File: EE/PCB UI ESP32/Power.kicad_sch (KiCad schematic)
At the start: 7 parts, among them J2 T1M-02-F-SV-L, U12 MCP1826ST-3302E_DB

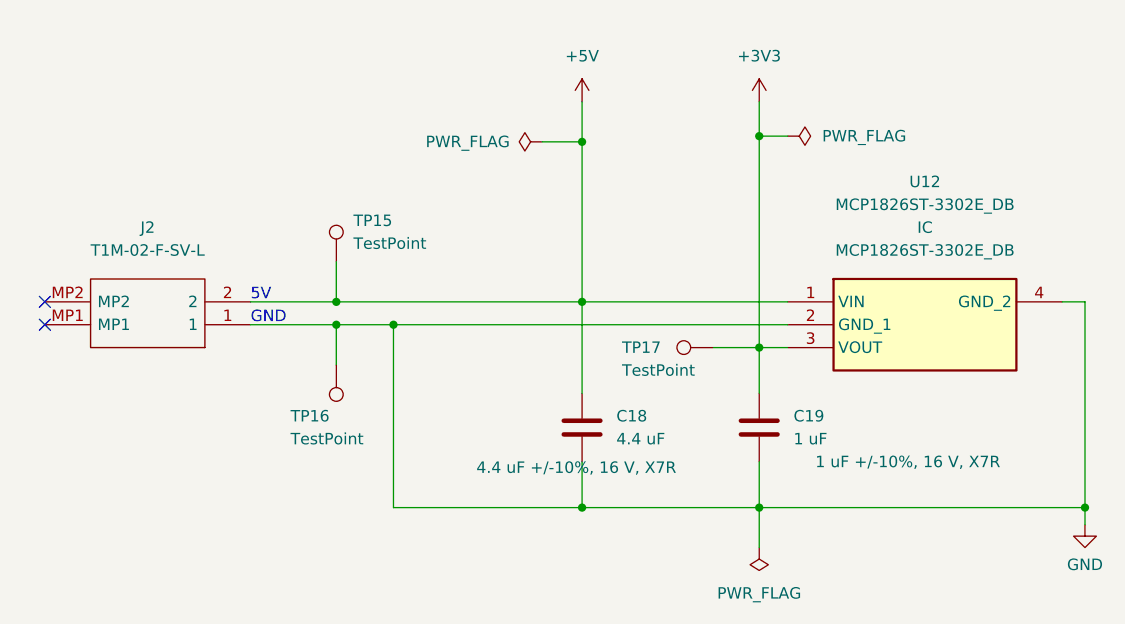
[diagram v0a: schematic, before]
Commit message: Finished first draft of ESP32-UI board
And moved around footprints, 3D models, etc. to match.
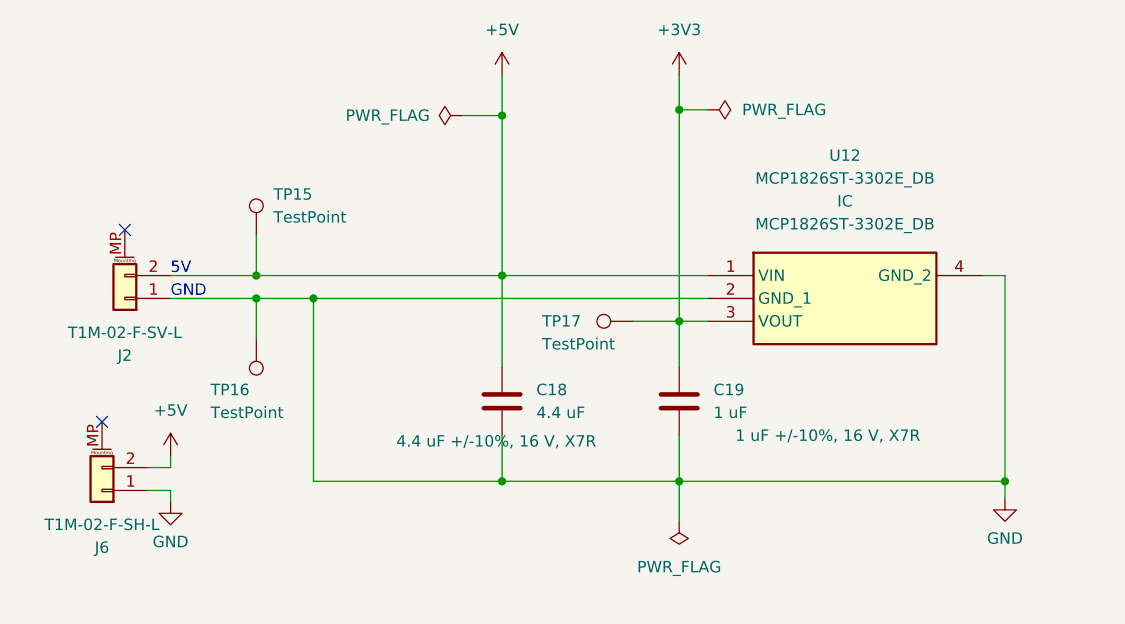
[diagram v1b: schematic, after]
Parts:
- removed J2: T1M-02-F-SV-L, T1M-02-F-SV-L:T1M02FSVL, symbol T1M-02-F-SV-L:T1M-02-F-SV-L
- added J2: T1M-02-F-SV-L, DaisyBio_Mira:T1M02FSVL, symbol Connector_Generic_MountingPin:Conn_01x02_MountingPin
- added J6: T1M-02-F-SH-L, DaisyBio_Mira:T1M-02-X-SH-L, symbol Connector_Generic_MountingPin:Conn_01x02_MountingPin
- U12: footprint MCP1826ST-3302E_DB:SOT230P700X180-4N -> DaisyBio_Mira:SOT230P700X180-4N
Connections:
- net +5V: now also J2.2 (Pin_2), J6.2 (Pin_2)
- net GND: now also J2.1 (Pin_1), J6.1 (Pin_1)
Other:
- moved on the sheet: C18, C19, TP15, TP16, TP17, U12
